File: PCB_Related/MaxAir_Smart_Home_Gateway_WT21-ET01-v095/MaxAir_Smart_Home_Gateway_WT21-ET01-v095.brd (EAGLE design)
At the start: 70 x 49 mm, 31 parts, among them J2 DCJ0202

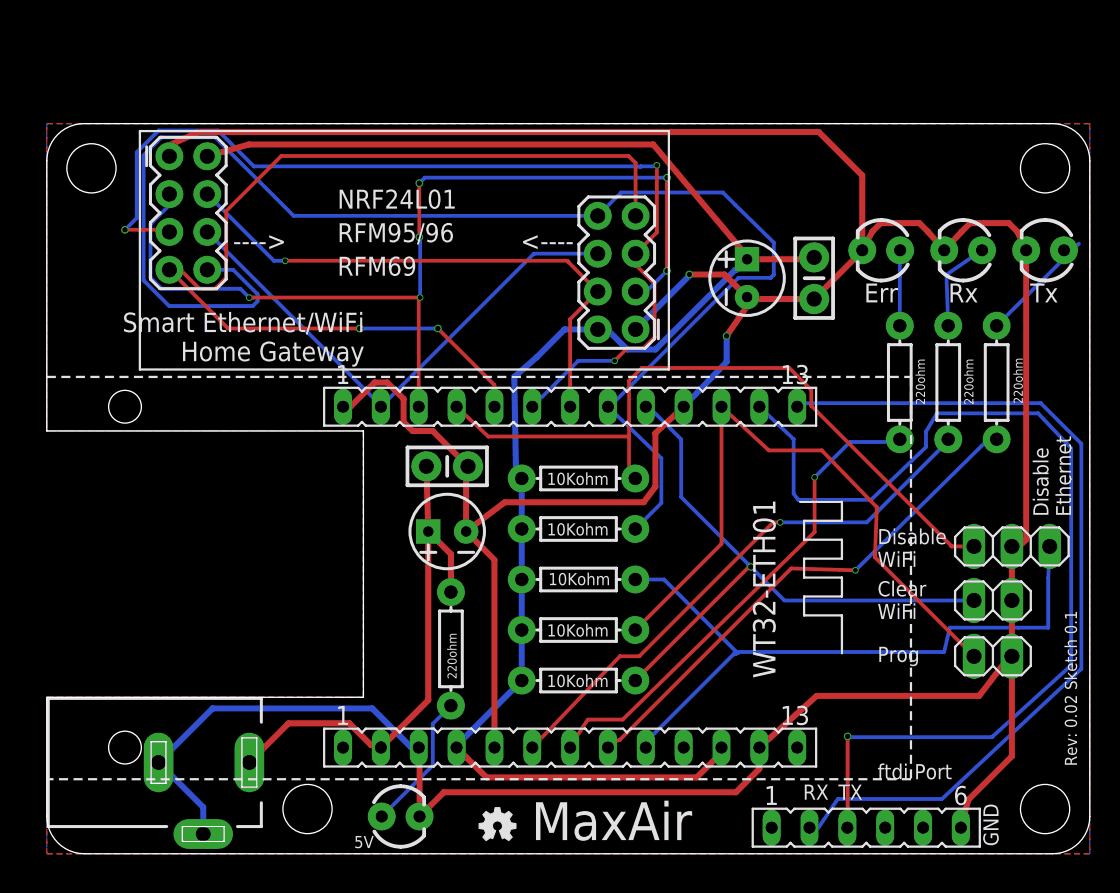
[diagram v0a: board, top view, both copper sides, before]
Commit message: MaxAir Smart Home Gateway
MaxAir Smart Home Gateway updates:
micro usb smd connector added, and power line traces width increased.
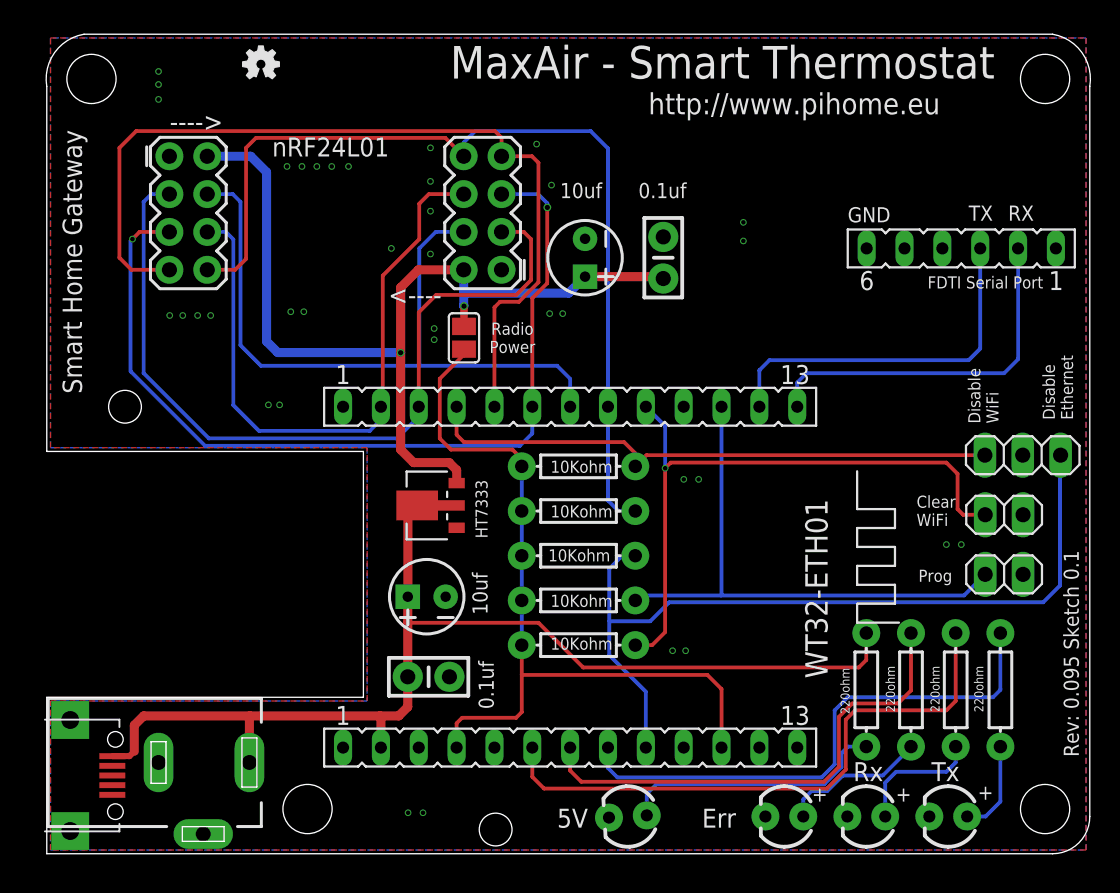
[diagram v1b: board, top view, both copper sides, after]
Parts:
- added IC2: HT7333, holtek2:SOT-89
- added SJ1: (no value), jumper:SJ
- added U$3: MICRO-USB, microusb:MICRO-USB
- moved LOGO1 53.5 mm to (14.4, 53.0)
- moved JP8 39.4 mm to (61.4, 40.6), turned to 180 degrees
- moved ERR 38.6 mm to (49.5, 2.50)
- moved RX 38.6 mm to (55.0, 2.50)
- moved TX 38.6 mm to (60.5, 2.50)
- moved R1 28.0 mm to (55.0, 11.0)
- moved R4 20.6 mm to (58.0, 11.0), turned to 90 degrees
- moved R3 20.6 mm to (61.0, 11.0), turned to 90 degrees
- moved R2 20.6 mm to (64.0, 11.0), turned to 90 degrees
- moved 5V 15.2 mm to (39.0, 2.50), turned to 183.3 degrees
- moved C4 14.2 mm to (25.6, 11.9)
- moved C1 11.0 mm to (36.1, 40.0), turned to 270 degrees
- moved C2 10.2 mm to (41.4, 40.0), turned to 90 degrees
- moved JP1 9.85 mm to (29.2, 43.0)
- moved JP7 6.17 mm to (65.5, 26.8)
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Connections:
- new net VCC_RADIO: C1.1, C2.1, IC2.1, JP1.2, JP2.2, SJ1.1
- net GND: now also IC2.2, U$3.5, U$3.GND1, U$3.GND2
- net VCC_3.3: now also SJ1.2; no longer C1.1, C2.1, JP1.2, JP2.2
- net VCC_5: now also IC2.3, IC2.4, U$3.1
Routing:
- net GND: track 264.7 -> 0.00 mm, vias 2 -> 37
- net VCC_RADIO: track 0.00 -> 63.9 mm, vias 0 -> 2
- net VCC_3.3: track 111.7 -> 53.9 mm
- net RX0: track 67.5 -> 24.6 mm, vias 1 -> 0
- net VCC_5: track 35.2 -> 75.7 mm, vias 1 -> 0
- net TX0: track 58.2 -> 24.5 mm
- net N_IRQ: track 95.8 -> 62.9 mm
- net N_CE: track 65.6 -> 54.7 mm, vias 6 -> 0
- net N_NSS: track 37.7 -> 48.3 mm, vias 1 -> 0
- net D_ETH: track 45.7 -> 55.1 mm
- net D_WIFI: track 48.2 -> 39.0 mm
- net N_MISO: track 68.3 -> 59.6 mm, vias 2 -> 0
- net N$1: track 9.36 -> 18.0 mm
- net N_SCK: track 68.0 -> 60.2 mm, vias 3 -> 2
- net PROG: track 44.2 -> 36.9 mm
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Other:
- board size 70 x 49 mm -> 70.1 x 55 mm
- board text added: "+"
- board text added: "5V"
- board text added: "FDTI Serial Port"
- board text added: "MaxAir - Smart Thermostat"
- board text added: "Radio Power"
- board text added: "Rev: 0.095 Sketch 0.1"
- board text added: "Smart Home Gateway"
- board text added: "nRF24L01"
- board text removed: "MaxAir"
- board text removed: "NRF24L01"
- board text removed: "PiHome - Smart Heating"
- board text removed: "RFM69"
- board text removed: "RFM95/96"
- board text removed: "Rev: 0.02 Sketch 0.1"
- board text removed: "Smart Ethernet/WiFi Home Gateway"
- board text removed: "ftdi Port"
